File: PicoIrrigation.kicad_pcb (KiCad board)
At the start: 2 copper layers, 165.1 x 88.9 mm, 178 parts, among them J1 M3, J10 I2C, J11 I2C, J12 I2C, J13 RSS232Out, J14 RSS232In, J15 SPI, J16 SPI, J17 V_{IN}, J18 UART8, J19 UART5, J2 M3, J20 UART6, J3 M3, J4 M3, J5 I2C, J6 I2C, J7 I2C, J8 I2C, J9 I2C, Q1 Q_PMOS_GSD, Q2 Q_PMOS_GSD, U1 Teensy4.1, U2 TCA9548APWR, U3 PCF8574TS, U4 MAX3232, U5 FM24CL16B

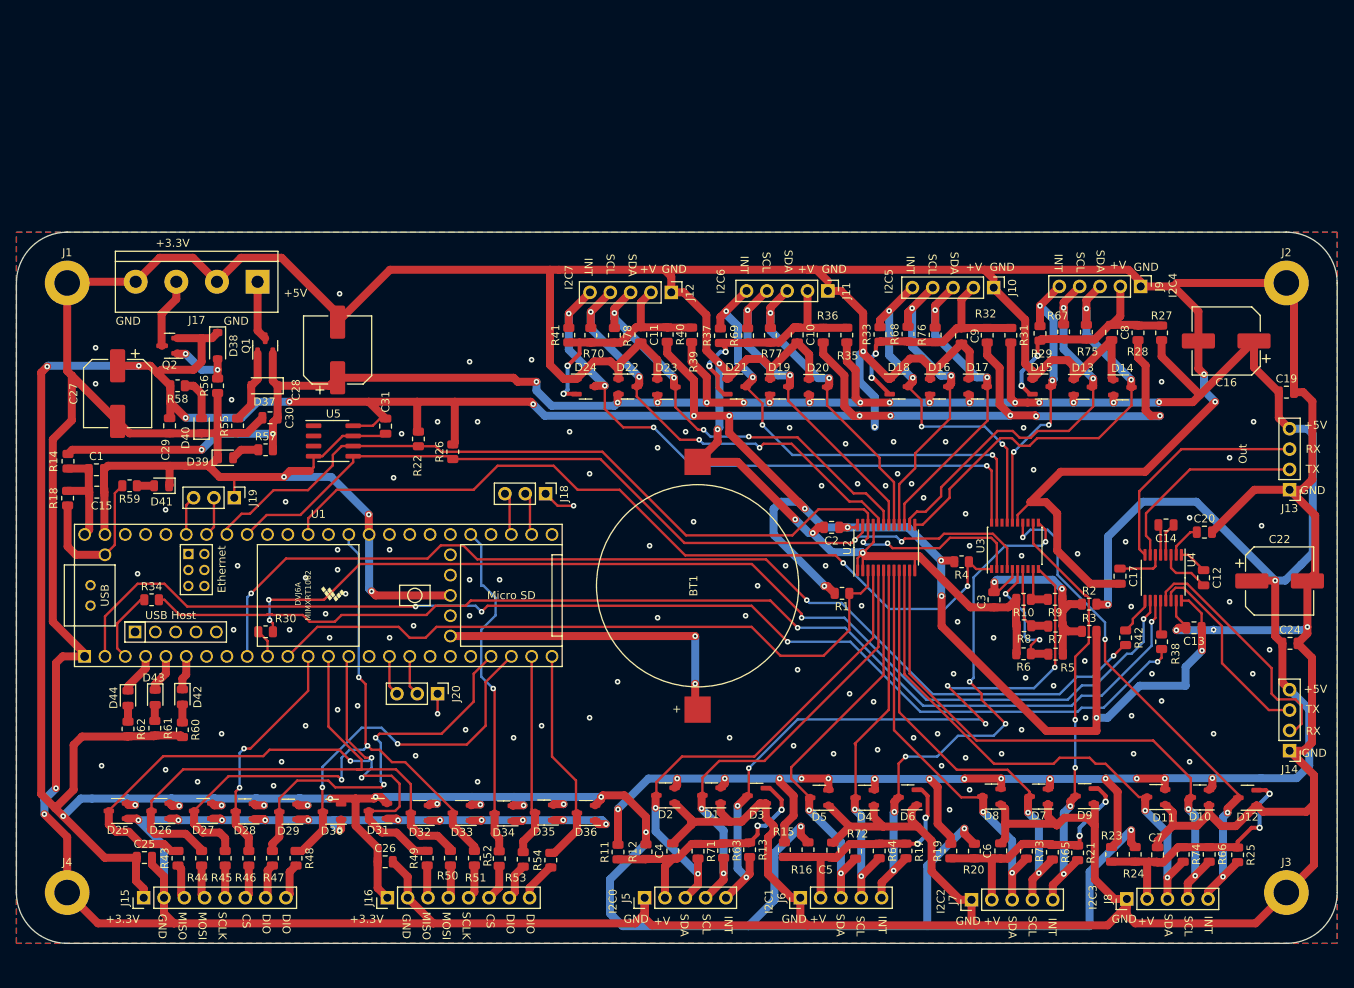
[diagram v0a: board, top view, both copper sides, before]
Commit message: Finished schematic. Move to PCB.
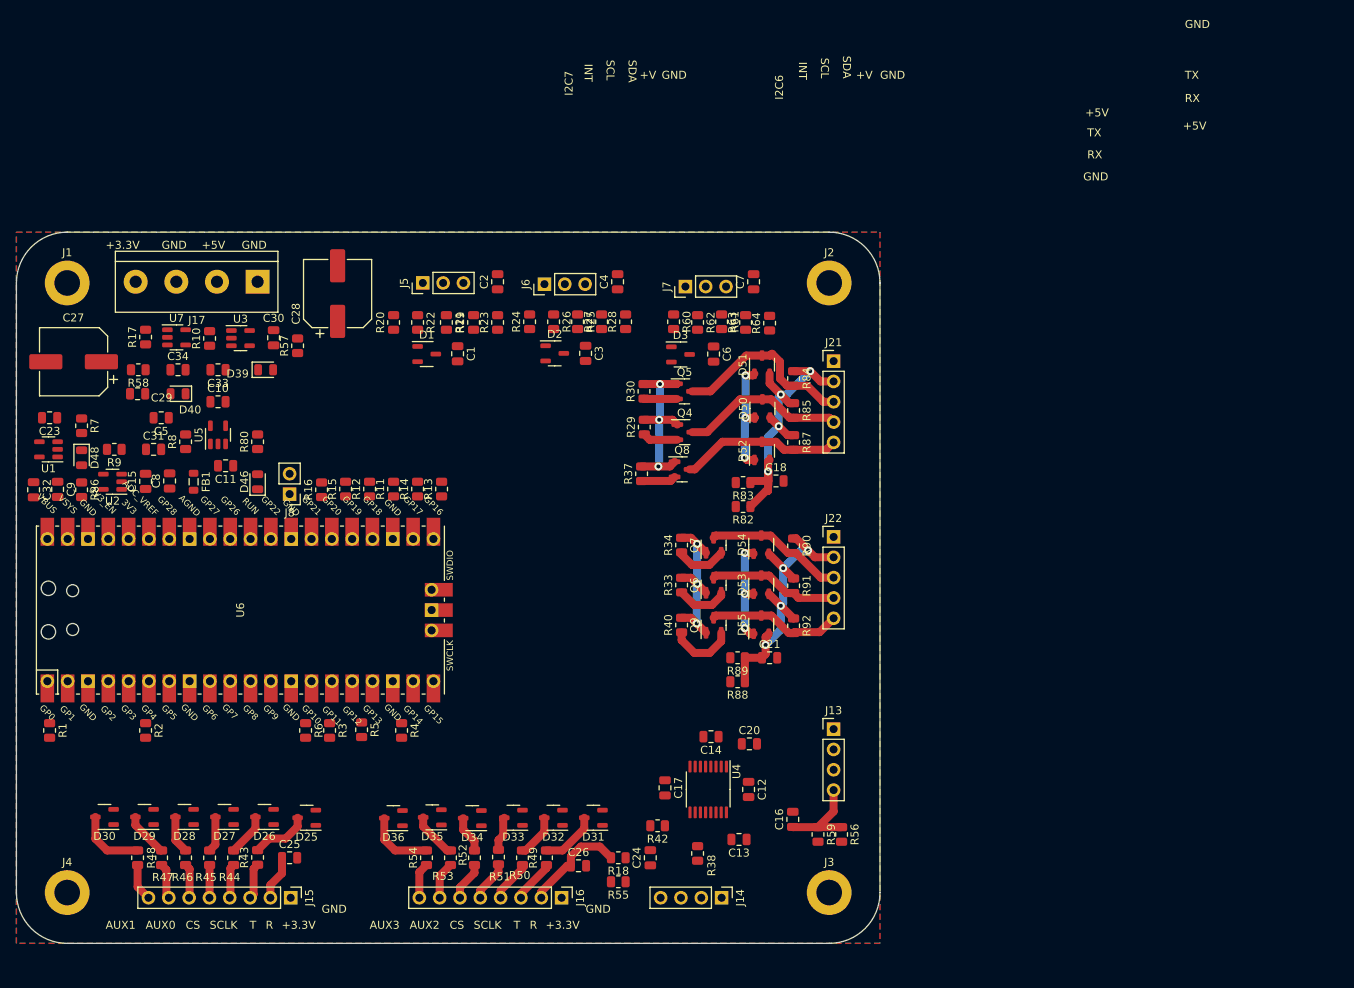
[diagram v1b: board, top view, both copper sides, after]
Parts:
- removed BT1: 2032Coin, BatteryCoin:BC2032
- removed C19: 1uF, Capacitor_SMD:C_0805_2012Metric
- removed C22: 100uF, Capacitor_SMD:CP_Elec_8x11.9
- removed D10, D11, D12, D13, D14, D15, D16, D17, D18, D19, D20, D21, D22, D23, D24, D4, D5, D6, D7, D8, D9: 100V, Package_TO_SOT_SMD:SOT-23-3
- removed D37, D38: 10V, Diode_SMD:D_SOD-123
- removed D41, D42, D43, D44: LED, LED_SMD:LED_0805_2012Metric
- removed J10, J11, J12, J9: I2C, Connector_PinHeader_2.54mm:PinHeader_1x05_P2.54mm_Vertical
- removed J18: UART8, Connector_PinHeader_2.54mm:PinHeader_1x03_P2.54mm_Vertical
- removed J19: UART5, Connector_PinHeader_2.54mm:PinHeader_1x03_P2.54mm_Vertical
- removed J20: UART6, Connector_PinHeader_2.54mm:PinHeader_1x03_P2.54mm_Vertical
- removed Q1, Q2: Q_PMOS_GSD, Package_TO_SOT_SMD:SOT-23
- removed R31, R32, R35, R36, R39: 0Ω, Resistor_SMD:R_0805_2012Metric
- removed R41, R65, R66, R67, R68, R69, R70, R71, R72, R73, R74, R75, R76, R77, R78: 10kΩ, Resistor_SMD:R_0805_2012Metric
- added C18: 1uF, Capacitor_SMD:C_0805_2012Metric, F.Cu at (164.8, 81.9)
- added C21: 1uF, Capacitor_SMD:C_0805_2012Metric, F.Cu at (164.0, 104.0)
- added C23: 1uF, Capacitor_SMD:C_0805_2012Metric, F.Cu at (74.0, 74.0)
- added C32: 10uF, Capacitor_SMD:C_0805_2012Metric, F.Cu at (72.0, 83.0)
- added C33: 1uF, Capacitor_SMD:C_0805_2012Metric, F.Cu at (95.0, 68.0)
- added C34: 1uF, Capacitor_SMD:C_0805_2012Metric, F.Cu at (90.0, 68.0)
- added D46: LED, LED_SMD:LED_0805_2012Metric, F.Cu at (100.0, 82.0)
- added D48: LED, LED_SMD:LED_0805_2012Metric, F.Cu at (78.0, 79.0)
- added D50: 100V, Package_TO_SOT_SMD:SOT-23-3, F.Cu at (163.1, 72.8)
- added D51: 100V, Package_TO_SOT_SMD:SOT-23-3, F.Cu at (163.1, 67.4)
- added D52: 100V, Package_TO_SOT_SMD:SOT-23-3, F.Cu at (163.1, 78.1)
- added D53: 100V, Package_TO_SOT_SMD:SOT-23-3, F.Cu at (162.9, 94.9)
- added D54: 100V, Package_TO_SOT_SMD:SOT-23-3, F.Cu at (162.9, 89.9)
- added D55: 100V, Package_TO_SOT_SMD:SOT-23-3, F.Cu at (162.9, 99.9)
- added FB1: NS_Ferrite, Inductor_SMD:L_0805_2012Metric, F.Cu at (92.0, 82.0)
- added J21: I2C, Connector_PinHeader_2.54mm:PinHeader_1x05_P2.54mm_Vertical, F.Cu at (172.0, 66.9)
- added J22: I2C, Connector_PinHeader_2.54mm:PinHeader_1x05_P2.54mm_Vertical, F.Cu at (172.0, 88.9)
- added Q4: Q_NMOS_GSD, Package_TO_SOT_SMD:SOT-23, F.Cu at (153.4, 75.8)
- added Q5: Q_NMOS_GSD, Package_TO_SOT_SMD:SOT-23, F.Cu at (153.4, 70.7)
- added Q6: Q_NMOS_GSD, Package_TO_SOT_SMD:SOT-23, F.Cu at (157.0, 94.9)
- added Q7: Q_NMOS_GSD, Package_TO_SOT_SMD:SOT-23, F.Cu at (157.0, 89.9)
- added Q8: Q_NMOS_GSD, Package_TO_SOT_SMD:SOT-23, F.Cu at (153.1, 80.5)
- added Q9: Q_NMOS_GSD, Package_TO_SOT_SMD:SOT-23, F.Cu at (157.0, 99.9)
- added R80: 500Ω, Resistor_SMD:R_0805_2012Metric, F.Cu at (100.0, 77.0)
- added R82: 0Ω, Resistor_SMD:R_0805_2012Metric, F.Cu at (160.7, 85.1)
- added R83: 0Ω, Resistor_SMD:R_0805_2012Metric, F.Cu at (160.7, 82.1)
- added R84: 10kΩ, Resistor_SMD:R_0805_2012Metric, F.Cu at (167.0, 69.1)
- added R85: 10kΩ, Resistor_SMD:R_0805_2012Metric, F.Cu at (167.0, 73.1)
- added R86: 500Ω, Resistor_SMD:R_0805_2012Metric, F.Cu at (78.0, 83.0)
- added R87: 10kΩ, Resistor_SMD:R_0805_2012Metric, F.Cu at (167.0, 77.1)
- added R88: 0Ω, Resistor_SMD:R_0805_2012Metric, F.Cu at (160.0, 107.0)
- added R89: 0Ω, Resistor_SMD:R_0805_2012Metric, F.Cu at (160.0, 104.0)
- added R90: 10kΩ, Resistor_SMD:R_0805_2012Metric, F.Cu at (167.0, 90.0)
- added R91: 10kΩ, Resistor_SMD:R_0805_2012Metric, F.Cu at (167.0, 95.0)
- added R92: 10kΩ, Resistor_SMD:R_0805_2012Metric, F.Cu at (167.0, 100.0)
- added U6: Pico, Pico:RPi_Pico_SMD_TH, F.Cu at (97.8, 98.0)
- added U7: MAX40200AUK, Package_TO_SOT_SMD:SOT-23-5, F.Cu at (89.9, 64.0)
- C10, C24, C5: value 1uF -> 10uF
- C16: value 100uF -> 10uF; footprint Capacitor_SMD:CP_Elec_8x11.9 -> Capacitor_SMD:C_0805_2012Metric
- J5, J6, J7: value I2C -> ADC; footprint Connector_PinHeader_2.54mm:PinHeader_1x05_P2.54mm_Vertical -> Connector_PinHeader_2.54mm:PinHeader_1x03_P2.54mm_Vertical
- J8: value I2C -> RUN; footprint Connector_PinHeader_2.54mm:PinHeader_1x05_P2.54mm_Vertical -> Connector_PinHeader_2.54mm:PinHeader_1x02_P2.54mm_Vertical
- R1, R13, R4, R5, R6: value 10kΩ -> 500Ω
- R10, R17, R7, R8, R9: value 10kΩ -> 100kΩ
- R11, R12, R14, R15, R16, R2, R3: value 0Ω -> 500Ω
- R18, R20, R23, R24, R28: value 0Ω -> NSΩ
- R21, R25, R64: value 10kΩ -> NSΩ
- R30, R34, R62: value 500Ω -> 10kΩ
- R40: value 0Ω -> 10kΩ
- R55, R56: value 100kΩ -> NSΩ
- R59, R60, R61: value 500Ω -> NSΩ
- R63: value 10kΩ -> 0Ω
- U1: value Teensy4.1 -> MAX40200AUK; footprint Teensy:Teensy41 -> Package_TO_SOT_SMD:SOT-23-5
- U2: value TCA9548APWR -> MAX40200AUK; footprint Package_SO:TSSOP-24_4.4x7.8mm_P0.65mm -> Package_TO_SOT_SMD:SOT-23-5
- U3: value PCF8574TS -> MAX40200AUK; footprint Package_SO:SSOP-20_4.4x6.5mm_P0.65mm -> Package_TO_SOT_SMD:SOT-23-5
- U5: value FM24CL16B -> MAX40200AUK; footprint Package_SO:SOIC-8_3.9x4.9mm_P1.27mm -> Package_TO_SOT_SMD:SOT-23-5
- moved R7 124.3 mm to (78.0, 75.0), turned to -90 degrees
- moved C8 119.2 mm to (89.0, 81.9), turned to 90 degrees
- moved R9 119.1 mm to (82.1, 78.0)
- moved R2 119.0 mm to (86.0, 113.1), turned to -90 degrees
- moved J8 116.2 mm to (104.0, 83.5), turned to 180 degrees
- moved R17 114.7 mm to (86.0, 63.9), turned to 90 degrees
- moved C9 114.6 mm to (75.0, 83.0)
- moved R8 107.3 mm to (91.0, 77.0), turned to 90 degrees
- moved R10 106.8 mm to (94.0, 64.1), turned to 90 degrees
- moved R25 106.1 mm to (140.0, 62.0)
- moved R21 103.1 mm to (123.6, 62.1)
- moved R23 101.5 mm to (130.0, 62.1)
- moved R24 100.8 mm to (134.0, 62.0)
- moved R1 100.5 mm to (74.0, 113.1), turned to -90 degrees
- moved U3 100.2 mm to (97.9, 64.0), turned to 0 degrees
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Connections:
- C1 pad 1: Net-(U1-VIN) -> /AnaloguePin/V_{A}
- C10 pad 1: /TCA9548AI2CMultiplexer/I2CConnector6/VBus -> +3.3V
- C11 pad 1: /TCA9548AI2CMultiplexer/I2CConnector7/VBus -> Net-(U5-EN)
- C15 pad 1: Net-(U1-VIN) -> +5V
- C16 pad 1: +5V -> Net-(J13-Pin_4)
- C2 pad 1: +3.3V -> Net-(J5-Pin_3)
- C24 pad 1: +5V -> Net-(J14-Pin_4)
- C3 pad 1: Net-(U3-VDD) -> /AnaloguePin1/V_{A}
- C31 pad 1: +3.3V -> Net-(U2-EN)
- C4 pad 1: /TCA9548AI2CMultiplexer/I2CConnector/VBus -> Net-(J6-Pin_3)
- C5 pad 1: /TCA9548AI2CMultiplexer/I2CConnector1/VBus -> Net-(U5-VDD)
- C6 pad 1: /TCA9548AI2CMultiplexer/I2CConnector2/VBus -> /AnaloguePin2/V_{A}
- C7 pad 1: /TCA9548AI2CMultiplexer/I2CConnector3/VBus -> Net-(J7-Pin_3)
- C8 pad 1: /TCA9548AI2CMultiplexer/I2CConnector4/VBus -> +5V
- C9 pad 1: /TCA9548AI2CMultiplexer/I2CConnector5/VBus -> Net-(U1-OUT)
- D1 pad 2: +5V -> +3.3V
- D1 pad 3: /TCA9548AI2CMultiplexer/I2CConnector/SCL -> /AnaloguePin/V_{A}
- D2 pad 2: +5V -> +3.3V
- D2 pad 3: /TCA9548AI2CMultiplexer/I2CConnector/SDA -> /AnaloguePin1/V_{A}
- D25 pad 3: /MISO -> /SPI_{Rx}0
- D26 pad 3: /MOSI -> /SPI_{Tx}0
- D27 pad 3: /SCLK -> /SCLK0
- D3 pad 2: /TCA9548AI2CMultiplexer/I2CConnector/VBus -> +3.3V
- D3 pad 3: /TCA9548AI2CMultiplexer/I2CConnector/INT -> /AnaloguePin2/V_{A}
- D31 pad 3: /MISO -> /SPI_{Rx}1
- D32 pad 3: /MOSI -> /SPI_{Tx}1
- D33 pad 3: /SCLK -> /SCLK1
- D34 pad 3: /CS1 -> /CS0
- J13 pad 4: +5V -> Net-(J13-Pin_4)
- J14 pad 4: +5V -> Net-(J14-Pin_4)
- J15 pad 1: +3.3V -> GND
- J15 pad 2: GND -> +3.3V
- J16 pad 1: +3.3V -> GND
- J16 pad 2: GND -> +3.3V
- J17 pad 1: Net-(J17-Pin_1) -> GND
- J17 pad 2: GND -> Net-(J17-Pin_2)
- J17 pad 3: Net-(J17-Pin_3) -> GND
- J17 pad 4: GND -> Net-(J17-Pin_4)
- J5 pad 2: /TCA9548AI2CMultiplexer/I2CConnector/VBus -> Net-(J5-Pin_2)
- J5 pad 3: /TCA9548AI2CMultiplexer/I2CConnector/SDA -> Net-(J5-Pin_3)
- J6 pad 2: /TCA9548AI2CMultiplexer/I2CConnector1/VBus -> Net-(J6-Pin_2)
- J6 pad 3: /TCA9548AI2CMultiplexer/I2CConnector1/SDA -> Net-(J6-Pin_3)
- J7 pad 2: /TCA9548AI2CMultiplexer/I2CConnector2/VBus -> Net-(J7-Pin_2)
- J7 pad 3: /TCA9548AI2CMultiplexer/I2CConnector2/SDA -> Net-(J7-Pin_3)
- J8 pad 2: /TCA9548AI2CMultiplexer/I2CConnector3/VBus -> Net-(J8-Pin_2)
- R1 pad 1: /~{RESET}I2C -> Net-(U6-GPIO0)
- R1 pad 2: +3.3V -> /TX0
- R10 pad 1: Net-(U3-A2) -> Net-(U3-EN)
- R10 pad 2: GND -> Net-(J17-Pin_2)
- R11 pad 1: /TCA9548AI2CMultiplexer/I2CConnector/VBus -> Net-(U6-GPIO18)
- R11 pad 2: +5V -> /SCLK0
- R12 pad 1: /TCA9548AI2CMultiplexer/I2CConnector/VBus -> Net-(U6-GPIO19)
- R12 pad 2: +3.3V -> /SPI_{Tx}0
- R13 pad 1: /TCA9548AI2CMultiplexer/I2CConnector/VBus -> Net-(U6-GPIO16)
- R13 pad 2: /TCA9548AI2CMultiplexer/I2CConnector/INT -> /SPI_{Rx}0
- R14 pad 1: +5V -> Net-(U6-GPIO17)
- R14 pad 2: Net-(U1-VIN) -> /CS0
- R15 pad 1: /TCA9548AI2CMultiplexer/I2CConnector1/VBus -> Net-(U6-GPIO20)
- R15 pad 2: +5V -> /AUX3
- R16 pad 1: /TCA9548AI2CMultiplexer/I2CConnector1/VBus -> Net-(U6-GPIO21)
- R16 pad 2: +3.3V -> /AUX2
- R17 pad 1: /TCA9548AI2CMultiplexer/I2CConnector1/VBus -> Net-(U7-EN)
- R17 pad 2: /TCA9548AI2CMultiplexer/I2CConnector1/INT -> Net-(J17-Pin_4)
- R18 pad 1: Net-(U1-VIN) -> Net-(J14-Pin_4)
- R18 pad 2: Net-(U1-VUSB) -> +3.3V
- R19 pad 1: /TCA9548AI2CMultiplexer/I2CConnector2/VBus -> +3.3V
- R19 pad 2: +5V -> Net-(J5-Pin_3)
- R2 pad 1: Net-(U3-VDD) -> Net-(U6-GPIO4)
- R2 pad 2: +5V -> /TX1
- R20 pad 1: /TCA9548AI2CMultiplexer/I2CConnector2/VBus -> /AnaloguePin/V_{A}
- R20 pad 2: +3.3V -> GND
- R21 pad 1: /TCA9548AI2CMultiplexer/I2CConnector2/VBus -> +3.3V
- R21 pad 2: /TCA9548AI2CMultiplexer/I2CConnector2/INT -> /AnaloguePin/V_{A}
- R22 pad 1: /SCL -> Net-(J5-Pin_2)
- R22 pad 2: +3.3V -> /AnaloguePin/V_{A}
- R23 pad 1: /TCA9548AI2CMultiplexer/I2CConnector3/VBus -> +5V
- R23 pad 2: +5V -> Net-(J5-Pin_3)
- R24 pad 1: /TCA9548AI2CMultiplexer/I2CConnector3/VBus -> /AnaloguePin1/V_{A}
- R24 pad 2: +3.3V -> GND
- R25 pad 1: /TCA9548AI2CMultiplexer/I2CConnector3/VBus -> +3.3V
- R25 pad 2: /TCA9548AI2CMultiplexer/I2CConnector3/INT -> /AnaloguePin1/V_{A}
- R26 pad 1: /SDA -> Net-(J6-Pin_2)
- R26 pad 2: +3.3V -> /AnaloguePin1/V_{A}
- R27 pad 1: /TCA9548AI2CMultiplexer/I2CConnector4/VBus -> +3.3V
- R27 pad 2: +5V -> Net-(J6-Pin_3)
- R28 pad 1: /TCA9548AI2CMultiplexer/I2CConnector4/VBus -> +5V
- R28 pad 2: +3.3V -> Net-(J6-Pin_3)
- R29 pad 1: /TCA9548AI2CMultiplexer/I2CConnector4/VBus -> /I2CConnector0/SCL
- R29 pad 2: /TCA9548AI2CMultiplexer/I2CConnector4/INT -> +3.3V
- R3 pad 1: Net-(U3-VDD) -> Net-(U6-GPIO11)
- R3 pad 2: +3.3V -> /SPI_{Tx}1
- R30 pad 1: Net-(U1-8_TX2_IN1) -> /I2CConnector0/SDA
- R30 pad 2: /TX1 -> +3.3V
- R33 pad 1: /TCA9548AI2CMultiplexer/I2CConnector5/VBus -> /I2CConnector1/SCL
- R33 pad 2: /TCA9548AI2CMultiplexer/I2CConnector5/INT -> +3.3V
- R34 pad 1: Net-(U1-1_TX1_CTX2_MISO1) -> /I2CConnector1/SDA
- R34 pad 2: /TX0 -> +3.3V
- R37 pad 1: /TCA9548AI2CMultiplexer/I2CConnector6/VBus -> /I2CConnector0/INT
- R37 pad 2: /TCA9548AI2CMultiplexer/I2CConnector6/INT -> +3.3V
- R4 pad 1: /TCA9548AI2CMultiplexer/~{INT} -> Net-(U6-GPIO13)
- R4 pad 2: +3.3V -> /CS0
- R40 pad 1: /TCA9548AI2CMultiplexer/I2CConnector7/VBus -> /I2CConnector1/INT
- R43 pad 2: /MISO -> /SPI_{Rx}0
- R44 pad 2: /MOSI -> /SPI_{Tx}0
- R45 pad 2: /SCLK -> /SCLK0
- R49 pad 2: /MISO -> /SPI_{Rx}1
- R5 pad 1: Net-(U3-VDD) -> Net-(U6-GPIO12)
- R5 pad 2: Net-(U3-A0) -> /SPI_{Rx}1
- R50 pad 2: /MOSI -> /SPI_{Tx}1
- R51 pad 2: /SCLK -> /SCLK1
- R52 pad 2: /CS1 -> /CS0
- R55 pad 1: GND -> Net-(J14-Pin_4)
- R55 pad 2: Net-(D37-A) -> +5V
- R56 pad 1: GND -> Net-(J13-Pin_4)
- R56 pad 2: Net-(D38-A) -> +3.3V
- R59 pad 1: Net-(D41-A) -> Net-(J13-Pin_4)
- R59 pad 2: Net-(U1-VUSB) -> +5V
- R6 pad 1: Net-(U3-A0) -> Net-(U6-GPIO10)
- R6 pad 2: GND -> /SCLK1
- R60 pad 1: Net-(D42-A) -> /AnaloguePin2/V_{A}
- R60 pad 2: +3.3V -> GND
- R61 pad 1: Net-(D43-A) -> +3.3V
- R61 pad 2: +3.3V -> /AnaloguePin2/V_{A}
- R62 pad 1: Net-(D44-A) -> Net-(J7-Pin_2)
- R62 pad 2: +3.3V -> /AnaloguePin2/V_{A}
- R63 pad 1: /TCA9548AI2CMultiplexer/I2CConnector/VBus -> +3.3V
- R63 pad 2: /TCA9548AI2CMultiplexer/I2CConnector/SCL -> Net-(J7-Pin_3)
- R64 pad 1: /TCA9548AI2CMultiplexer/I2CConnector1/VBus -> +5V
- R64 pad 2: /TCA9548AI2CMultiplexer/I2CConnector1/SCL -> Net-(J7-Pin_3)
- R7 pad 1: Net-(U3-VDD) -> Net-(U1-EN)
- R7 pad 2: Net-(U3-A1) -> Net-(U1-VDD)
- R8 pad 1: Net-(U3-A1) -> Net-(U5-EN)
- R8 pad 2: GND -> Net-(U5-VDD)
- R9 pad 1: Net-(U3-VDD) -> Net-(U2-EN)
- R9 pad 2: Net-(U3-A2) -> +5V
- U1 pad 1: GND -> Net-(U1-VDD)
- U1 pad 2: /RX0 -> GND
- U1 pad 3: Net-(U1-1_TX1_CTX2_MISO1) -> Net-(U1-EN)
- U1 pad 4: Net-(D44-K) -> unconnected-(U1-NC-Pad4)
- U1 pad 5: Net-(D43-K) -> Net-(U1-OUT)
- U2 pad 1: GND -> +5V
- U2 pad 3: /~{RESET}I2C -> Net-(U2-EN)
- U2 pad 4: /TCA9548AI2CMultiplexer/I2CConnector/SDA -> unconnected-(U2-NC-Pad4)
- U2 pad 5: /TCA9548AI2CMultiplexer/I2CConnector/SCL -> Net-(U1-OUT)
- U3 pad 1: /TCA9548AI2CMultiplexer/~{INT} -> Net-(J17-Pin_2)
- U3 pad 2: /SCL -> GND
- U3 pad 3: unconnected-(U3-NC-Pad3) -> Net-(U3-EN)
- U3 pad 4: /SDA -> unconnected-(U3-NC-Pad4)
- U3 pad 5: Net-(U3-VDD) -> +5V
- U5 pad 1: unconnected-(U5-Pad1) -> Net-(U5-VDD)
- U5 pad 2: unconnected-(U5-Pad2) -> GND
- U5 pad 3: unconnected-(U5-Pad3) -> Net-(U5-EN)
- U5 pad 4: GND -> unconnected-(U5-NC-Pad4)
- U5 pad 5: /SDA -> +3.3V
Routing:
- net GND: track 1212.6 -> 27.0 mm, vias 141 -> 6
- net +3.3V: track 694.0 -> 63.4 mm, vias 36 -> 6
- net +5V: track 441.7 -> 0.00 mm, vias 35 -> 0
- net /RX0: track 150.0 -> 0.00 mm, vias 4 -> 0
- net /TX0: track 140.8 -> 0.00 mm, vias 2 -> 0
- net /TX1: track 131.2 -> 0.00 mm, vias 4 -> 0
- net /RX1: track 130.1 -> 0.00 mm, vias 3 -> 0
- net /SCL: track 117.1 -> 0.00 mm, vias 2 -> 0
- net /SDA: track 110.7 -> 0.00 mm, vias 2 -> 0
- net /TCA9548AI2CMultiplexer/~{INT}: track 102.1 -> 0.00 mm, vias 2 -> 0
- net /MISO: track 88.2 -> 0.00 mm, vias 3 -> 0
- net /TCA9548AI2CMultiplexer/I2CConnector/INT: track 87.8 -> 0.00 mm, vias 6 -> 0
- net /~{RESET}I2C: track 84.9 -> 0.00 mm
- net /SCLK: track 82.5 -> 0.00 mm, vias 3 -> 0
- net /TCA9548AI2CMultiplexer/I2CConnector7/INT: track 78.7 -> 0.00 mm, vias 4 -> 0
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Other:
- board size 165.1 x 88.9 mm -> 108 x 88.9 mm
- board text added: "AUX0"
- board text added: "AUX1"
- board text added: "AUX2"
- board text added: "AUX3"
- board text added: "R"
- board text added: "T"
- board text removed: "DIO"
- board text removed: "I2C0"
- board text removed: "I2C1"
- board text removed: "I2C2"
- board text removed: "I2C3"
- board text removed: "I2C4"
- board text removed: "I2C5"
- board text removed: "MISO"
- board text removed: "MOSI"
- board text removed: "Out"

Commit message: Finished layout
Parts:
- moved R4 1.80 mm to (116.2, 113.0)
- moved C5 0.99 mm to (87.2, 74.7)
- moved R8 0.51 mm to (91.5, 77.1), turned to -90 degrees
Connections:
- D34 pad 3: /CS0 -> /CS1
- R4 pad 2: /CS0 -> /CS1
- R52 pad 2: /CS0 -> /CS1
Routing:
- net GND: track 27.0 -> 951.0 mm, vias 6 -> 93
- net +3.3V: track 63.4 -> 399.4 mm, vias 6 -> 31
- net +5V: track 0.00 -> 248.1 mm, vias 0 -> 13
- net /I2CConnector0/INT: track 4.34 -> 104.5 mm, vias 0 -> 1
- net /RX0: track 0.00 -> 96.1 mm, vias 0 -> 3
- net /AnaloguePin2/V_{A}: track 0.00 -> 94.3 mm, vias 0 -> 2
- net /TX0: track 0.00 -> 91.5 mm, vias 0 -> 4
- net /I2CConnector0/SDA: track 4.14 -> 83.0 mm, vias 0 -> 1
- net /I2CConnector0/SCL: track 4.40 -> 83.1 mm, vias 0 -> 1
- net /TX1: track 0.00 -> 78.6 mm, vias 0 -> 4
- net /I2CConnector1/INT: track 8.26 -> 81.6 mm, vias 0 -> 1
- net /CS0: track 9.34 -> 81.8 mm, vias 0 -> 2
- net /RX1: track 0.00 -> 70.2 mm
- net /SCLK0: track 4.49 -> 73.4 mm, vias 0 -> 2
- net /I2CConnector1/SCL: track 6.45 -> 74.8 mm, vias 0 -> 1
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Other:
- board text added: "A0"
- board text added: "A1"
- board text added: "A2"
- board text added: "I2C0"
- board text added: "I2C1"
- board text added: "RS_{232}0"
- board text added: "RS_{232}1"
- board text added: "R_{IN}"
- board text added: "SPI1"
- board text added: "T_{OUT}"
- board text added: "V_{A}"
- board text removed: "I2C6"
- board text removed: "I2C7"
- board text removed: "RX"
- board text removed: "TX"

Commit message: Ready V1
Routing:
- net GND: track 951.0 -> 947.2 mm
